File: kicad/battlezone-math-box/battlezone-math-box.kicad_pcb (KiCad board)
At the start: 2 copper layers, 170 x 265 mm, 34 parts

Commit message: Read sheet 1 Side B, and let it correct three sheets and me
Sheet 1 Side B turned out to be the most useful sheet in the package: the
whole Auxiliary PCB signature analysis procedure, plus four figures that
print each signature against the device pin it belongs to -- and printed,
not hand-lettered. 113 pin-level signatures across the four tests are now
recorded exactly, for both Battlezone and Red Baron.

Its Figure 1 is a test-point map of the board, and checking my sheet 3
Side B read against it found two devices I had missed: E1 and D1, a pair
of LS161s. They are not incidental. They are the microcode program
counter -- B1 supplies an entry address, E1 and D1 latch it and then step,
and their eight outputs are the address bus for the six microcode PROMs.
The sequencer only makes sense with them in it, and last commit's claim
that the sheet was fully read was wrong.

The typeset figures also settle every conflict I logged last time. The two
printings of sheet 3 Side B disagreed about a signature box; Figure 2B
gives the same signatures per device pin and confirms the 2nd printing,
so the 1st printing simply prints that column reversed. 1F47/9F47,
3UF3/3U53, 4569/9569 and 2P41/2P61 all resolve the same way.

One of those corrections is to my own reasoning. I had read a code as
"CAPE", argued from the analyser's alphabet that E is not a legal
character so it must be a 5, and recorded CAP5. Figure 2A prints C4P5. The
alphabet argument was right that the reading was impossible and wrong
about what replaced it -- a constraint that rejects a reading does not
thereby produce the correct one.

And a correction to my last correction. I said the published shared-Math-
Box note "gave the PROMs as L1 through E1". It did not; it listed device
positions without claiming what they were, and I misrepresented it. What
is actually wrong with it is narrower: it omits M1 and it garbles the four
ALU slices. Restated fairly, in both signature records.

Still unresolved and logged: Figu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
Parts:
- added UD1: 74LS161, DIP-14_W7.62mm, F.Cu at (26.0, 170.4)
- added UE1: 74LS161, DIP-14_W7.62mm, F.Cu at (26.0, 151.3)

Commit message: Draw every device at its real package size
The board maps existed to answer "which chip is at C4", and then drew a
24-pin ROM and a 20-pin LS245 as the same 14-pin outline. package_for()
read pin counts from DEVICES, which holds 20 Pong-era parts against the
112 part types the boards actually use, and silently fell back to DIP-14
for the other 92.

tools/packages.py is the pin-count table, kept separate from devices.py
on purpose: packaging needs one number for every part on every board,
while devices.py carries verified pinouts for the parts validate_nets.py
reasons about, and widening that set to satisfy a drawing would let the
extractor trust readings nothing has checked.

688 of 704 devices now size. check_packages.py re-derives 56 of the
entries from KiCAD's symbol library — comparing the highest pin number,
not the pin count, since KiCAD omits no-connects and a 7493 symbol has
ten pins on a DIP-14 — and confirms all 20 parts in DEVICES agree. The
Am2901 slices and the POKEY come from DIP-40 stated on the Battlezone
sheet; the 8316E from the drawing's note that a 2708 may be fitted
instead.

What does not size is now said out loud rather than quietly drawn at 14
pins: four descriptions recorded where the sheet gave no part number,
and the Atari 0351xx ROM/PROM numbers, which get the class default and
are listed as unverified until someone has a board in front of them.

Two things found while reading the corpus for packages, both logged in
asteroids.read.json rather than acted on. The -06 rate multiplier
resolution was recorded and never applied to the board data, and the
parts list disagrees with both readings on designators. F4/H4/J4 take
either an LS670 or an LS170, and the 19-007 pull-up network is fitted
only with the LS170 — same package either way, but a real failure mode.

Also: republishing a board without --machine used to unlink it from its
machine, because most definitions carry no machine of their own and the
link lived only in boards.json. publish_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
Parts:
- UB1, UB4, UC3, UD1, UE1, UF1, UF4, UF5, UH1, UJ1, UK1, UL1, UM1: footprint DIP-14_W7.62mm -> DIP-16_W7.62mm
- UB2, UD2, UF2, UH2, UK2: footprint DIP-14_W7.62mm -> DIP-40_W15.24mm
- UC1, UM2: footprint DIP-14_W7.62mm -> DIP-20_W7.62mm

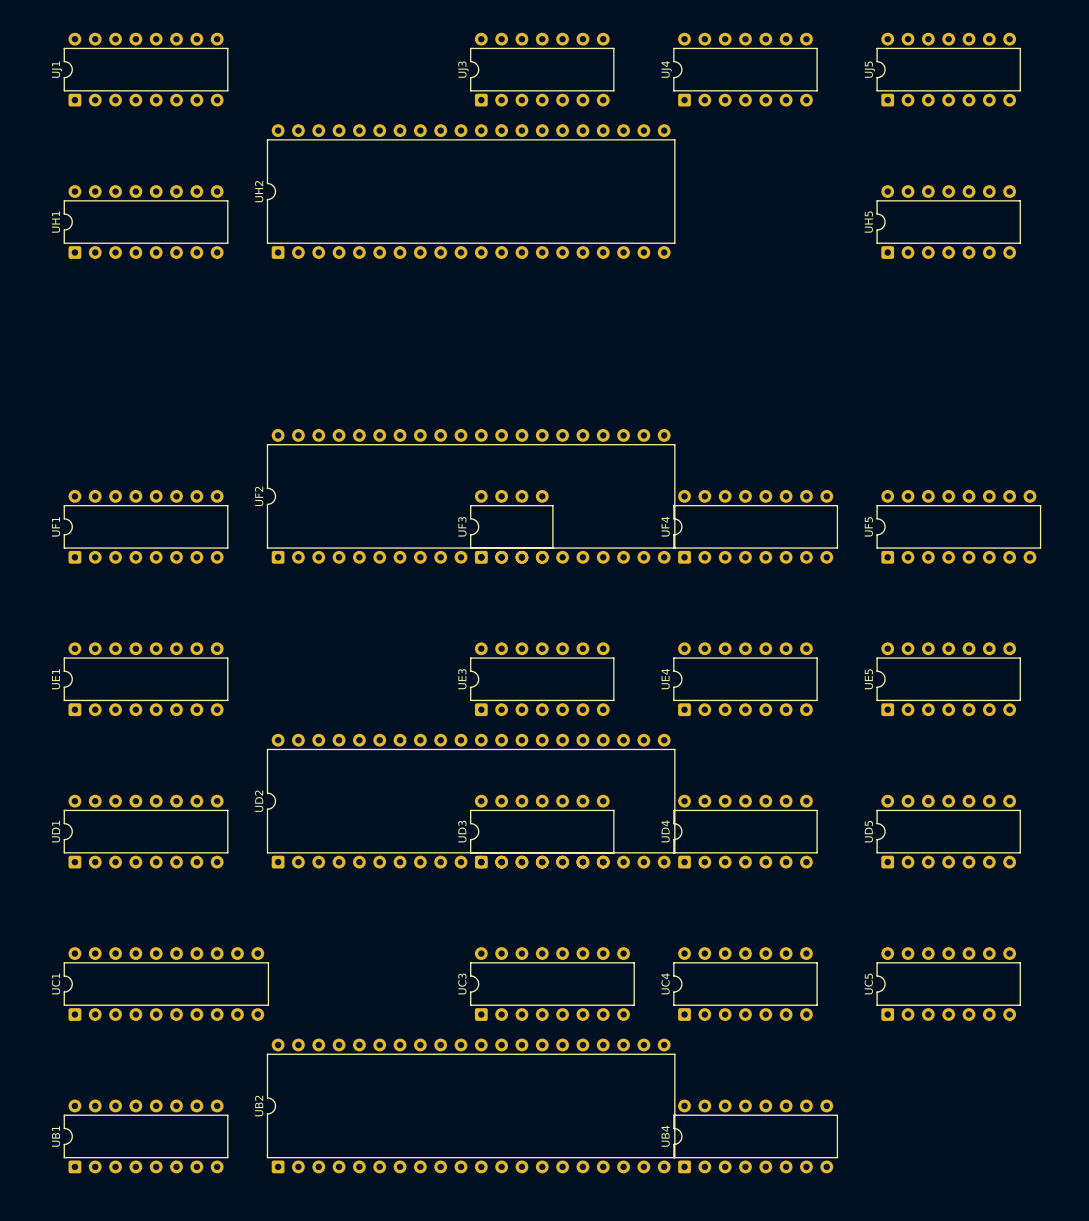
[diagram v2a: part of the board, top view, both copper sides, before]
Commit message: Drop two grid rows that do not exist, and span the devices that do
Atari's grid alphabet skips G, I, O and Q, and the board definitions
listed G and Q as rows. Every device below F was therefore drawn a row
too low, the rendered board carried two empty bands, and F/H1 looked
like a three-position span for a part 1.2in long on a 0.75in pitch.

Confirmed three ways before touching it. Nothing in any read, signature
or signal record in this repo sits in a G or Q row, while both
neighbours of each are populated on the two densest boards — Battlezone
P:6 R:2, Asteroids-03 P:4 R:3. The sheets' own spanning designators
treat F and H as adjacent and H and J as adjacent, which is only
possible if G and I are not positions. And with G removed, F/H falls out
as an adjacent pair, which is what a 24-pin ROM needs. Pong predates the
convention and legitimately uses G, so it keeps its grid.

Spans are now data rather than prose. A device drawn across two or three
cells is still keyed at its first cell, because that is the only thing
`ics` may be keyed by, but the sheet's own designator goes in a `spans`
map and the footprint is placed at the mean of the cells it names. A
DIP-40 at B/C2 sits between B2 and C2 instead of hanging equally over A2
and C2. The build rejects a span whose rows are not adjacent — that
failure almost always means the grid is wrong, not the span.

Two more inconsistencies found and logged rather than guessed at. Two of
the Math Box's four Am2901 slices carry a span and two do not, though
all four are the same DIP-40 on the same pitch. And asteroids-04.json
carries five devices at the -03 PROM positions alongside the -04 ROMs
and is missing 035144-02 at D/E1, contradicting the substitution table,
memory_by_revision and its own status text in the same breath.

Co-Authored-By: Claude Opus 5 <noreply@anthropic.com>
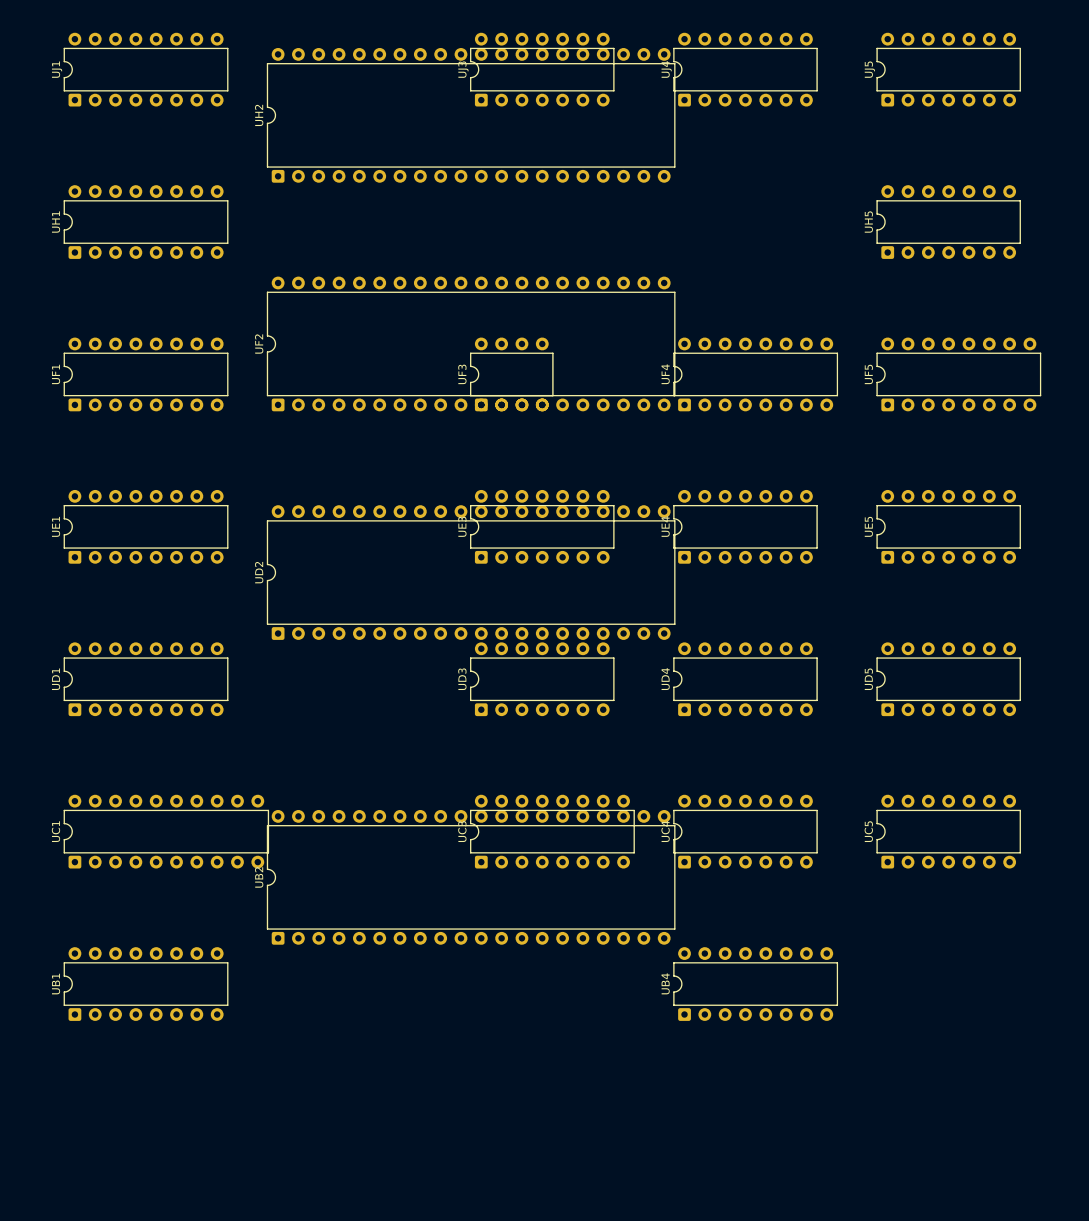
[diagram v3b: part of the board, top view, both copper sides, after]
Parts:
- moved UD2 28.6 mm to (51.4, 141.8)
- moved UB2 28.6 mm to (51.4, 179.9)
- moved UB1 19.1 mm to (26.0, 189.4)
- moved UB4 19.1 mm to (102.2, 189.4)
- moved UD1 19.1 mm to (26.0, 151.3)
- moved UD3 19.1 mm to (76.8, 151.3)
- moved UD4 19.1 mm to (102.2, 151.3)
- moved UD5 19.1 mm to (127.6, 151.3)
- moved UF1 19.1 mm to (26.0, 113.2)
- moved UF2 19.1 mm to (51.4, 113.2)
- moved UF3 19.1 mm to (76.8, 113.2)
- moved UF4 19.1 mm to (102.2, 113.2)
- moved UF5 19.1 mm to (127.6, 113.2)
- moved UC1 19.0 mm to (26.0, 170.4)
- moved UC3 19.0 mm to (76.8, 170.4)
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
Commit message: Split multi-PCB manuals by figure, and take Battlezone through
A manual covering more than one PCB gives each its own parts-list figure,
and the heading names the board. Without using that, Battlezone's two
boards land in one heap and their designators collide — which AGENTS.md
already warns about in the drawings: C1 on one is not C1 on the other,
and both have a +5V LED called CR2. Rows now carry the figure they sit
under and --figure filters on it.

Battlezone is the result worth trusting the method on. It is the most
carefully hand-read board in the project, 97 devices off six sheet
sides, and across both PCBs the parts lists confirm 87 of 87 overlapping
designators with no disagreement at all. That says the harvest is sound
and that the six-sheet read was, and it recasts the 21 disagreements on
Asteroids as more likely errors in that read than noise in the lists.
The game PCB gains 8 devices and the Auxiliary 1 — small numbers, but
the confirmation is the point.

Also fixes a real loss this merge caused on its first run. The chip
lookup holds more than `ics` does: crystals, transistors, resistor
packs, a test point — everything on the board that is not on the
letter-number grid and so cannot be drawn. Rebuilding the lookup from
`ics` alone dropped twelve hand-read Battlezone devices and one on the
Auxiliary PCB. They are carried through now, and the hazard is written
into AGENTS.md next to the warning I had already put there and then
walked straight into.

Co-Authored-By: Claude Opus 5 <noreply@anthropic.com>
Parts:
- added UH4: 74LS164, DIP-14_W7.62mm, F.Cu at (102.2, 94.2)
